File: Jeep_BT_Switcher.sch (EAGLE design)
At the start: 26 parts, among them J1 MF-CON-2.54mm-01x06, J2 MF-CON-2.54mm-01x04, U1 AZ4558C, U2 MAX4544CSA+, U3 MAX4544CSA+

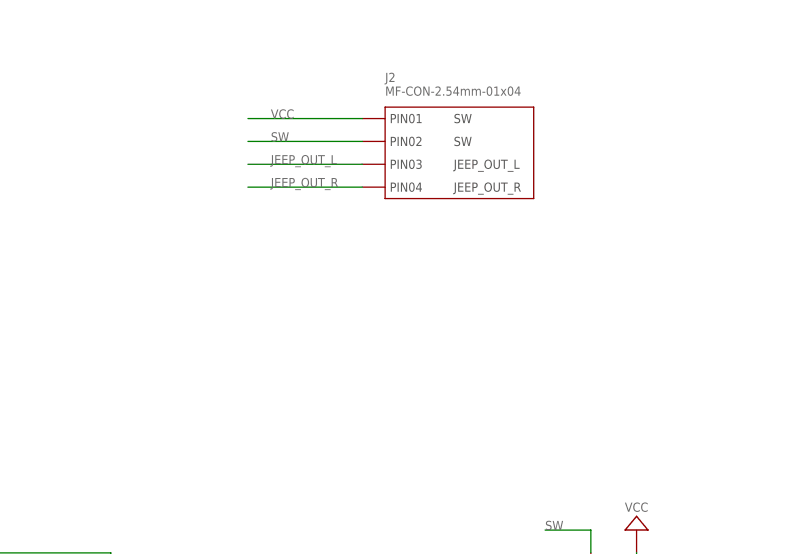
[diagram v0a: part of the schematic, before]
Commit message: Added EXT power connector.
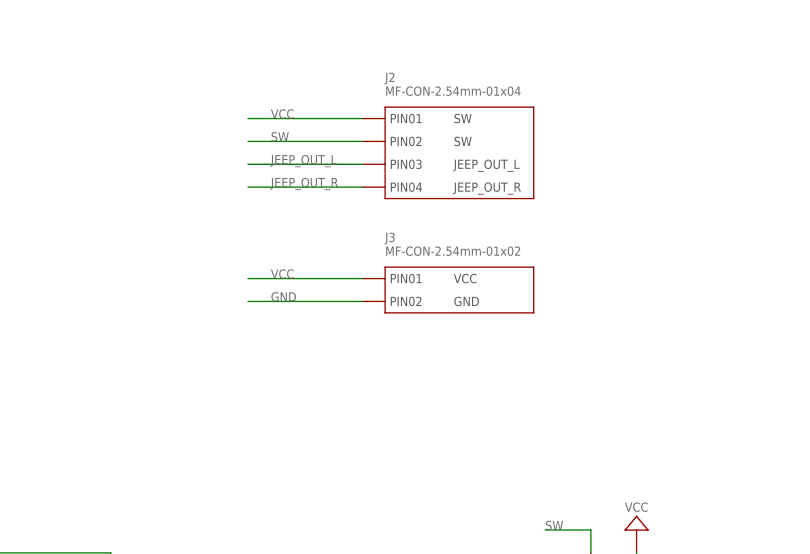
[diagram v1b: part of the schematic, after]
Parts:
- added J3: MF-CON-2.54mm-01x02, MF_Connectors:CON_01X02_PTH_2.54MM
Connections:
- net GND: now also J3.PIN2
- net VCC: now also J3.PIN1
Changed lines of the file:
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@@
 <part name="H4" library="PP_Connectors" deviceset="MOUNT_HOLE" device="150MIL"/>
 <part name="C7" library="MF_Passives" deviceset="CAPACITOR_NP" device="_0805" value="0.1uF"/>
+<part name="J3" library="MF_Connectors" deviceset="CON_01X02" device="_PTH_2.54MM" value="MF-CON-2.54mm-01x02">
+<attribute name="LABEL01" value="VCC"/>
+<attribute name="LABEL02" value="GND"/>
+</part>
 </parts>
 <sheets>
@@
 <instance part="H4" gate="G$1" x="203.2" y="58.42"/>
 <instance part="C7" gate="G$1" x="7.62" y="86.36" rot="MR0"/>
+<instance part="J3" gate="G$1" x="99.06" y="124.46"/>
 </instances>
 <busses>
@@
 <junction x="127" y="35.56"/>
 <label x="129.54" y="35.56" size="1.016" layer="95" font="vector"/>
+</segment>
+<segment>
+<pinref part="J3" gate="G$1" pin="PIN1"/>
+<wire x1="96.52" y1="124.46" x2="83.82" y2="124.46" width="0.1524" layer="91"/>
+<label x="86.36" y="124.46" size="1.016" layer="95" font="vector"/>
 </segment>
 </net>
@@
 <label x="129.54" y="17.78" size="1.016" layer="95" font="vector"/>
 </segment>
+<segment>
+<pinref part="J3" gate="G$1" pin="PIN2"/>
+<wire x1="83.82" y1="121.92" x2="96.52" y2="121.92" width="0.1524" layer="91"/>
+<label x="86.36" y="121.92" size="1.016" layer="95" font="vector"/>
+</segment>
 </net>

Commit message: Added cam files and XYRS
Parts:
- added U$11: LHE_FRAME, PP_Aesthetics:LHE_FRAME
- added U$12: MF_LOGOLOGO_SMALL, PP_Aesthetics:MF_LOGOLOGO_SMALL
- added U$13: LHE_LOGOLHE_LOGO, PP_Aesthetics:LHE_LOGOLHE_LOGO
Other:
- moved on the sheet: C1, C2, C3, C4, C5, C6, C7, H1, H2, H3, H4, J1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

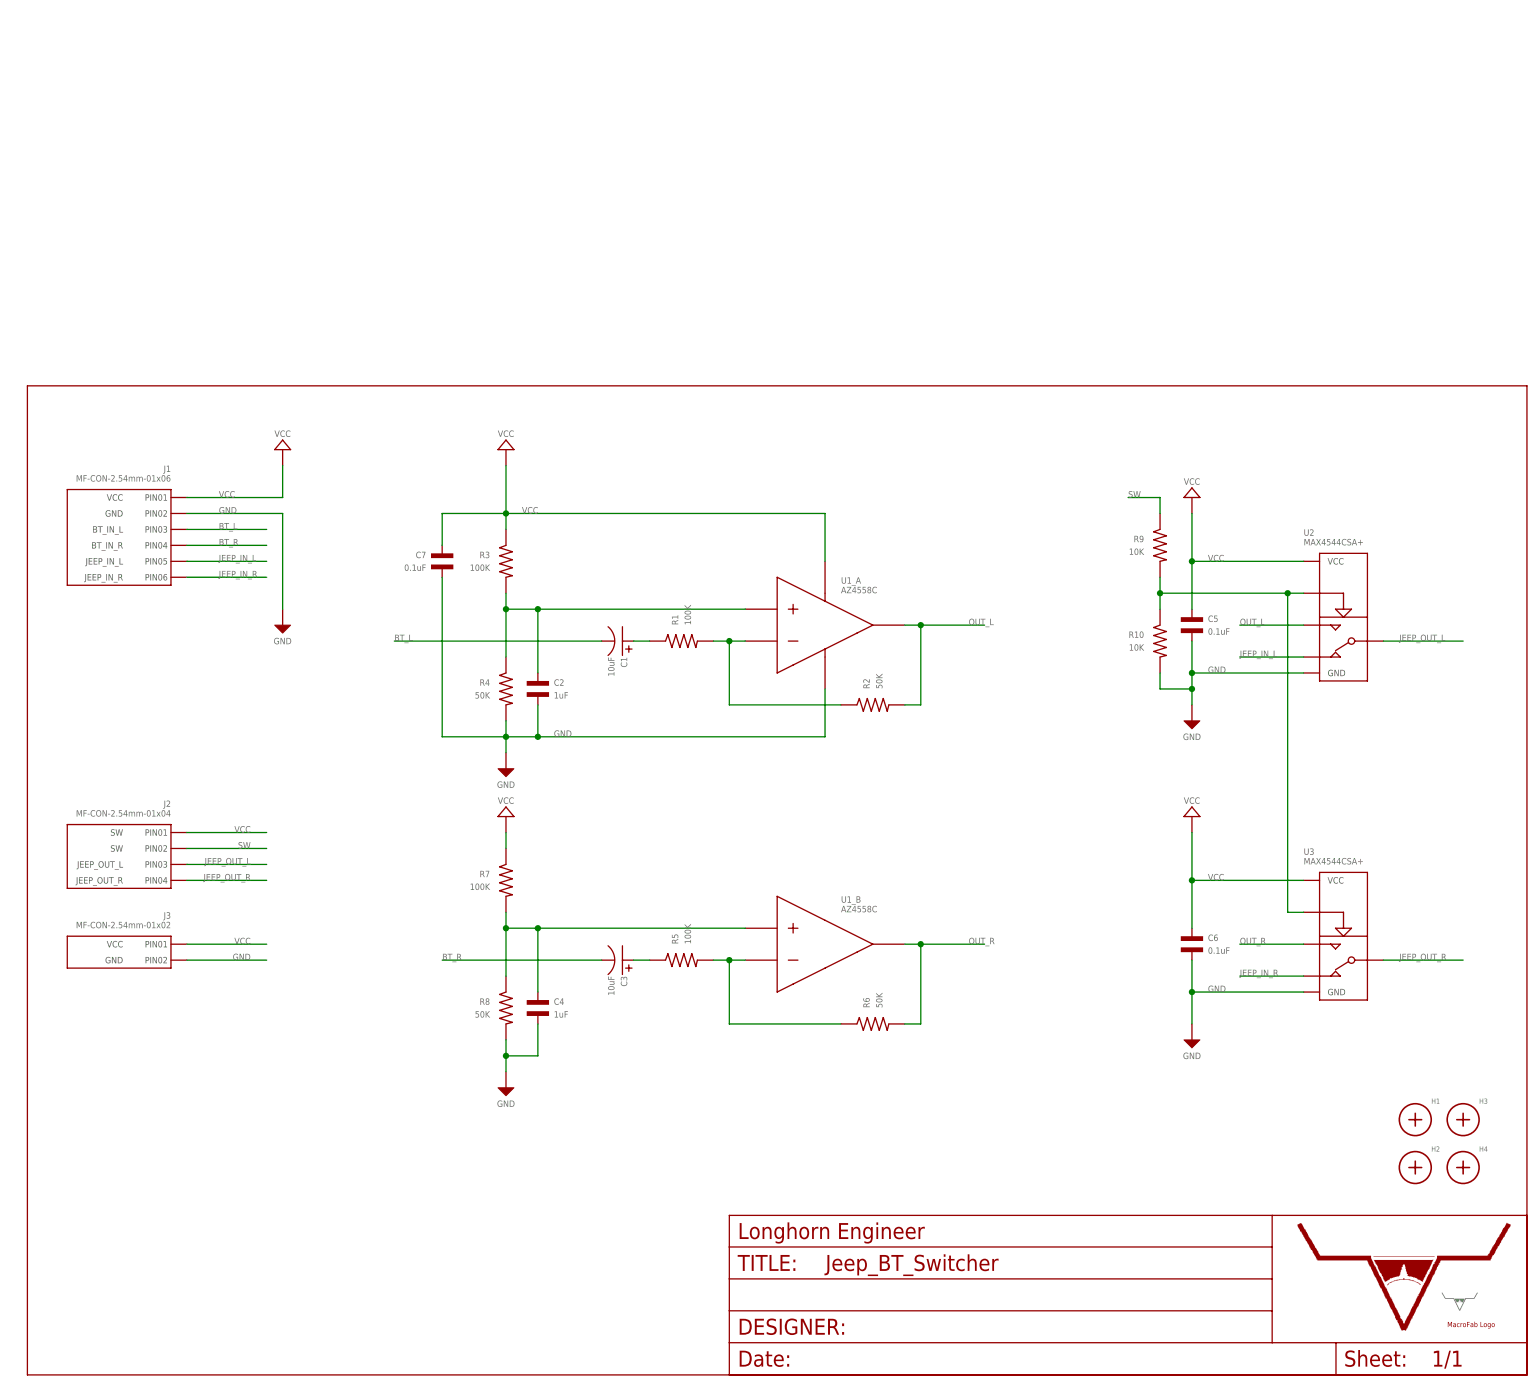
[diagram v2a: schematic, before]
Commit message: Adding built in BT module.
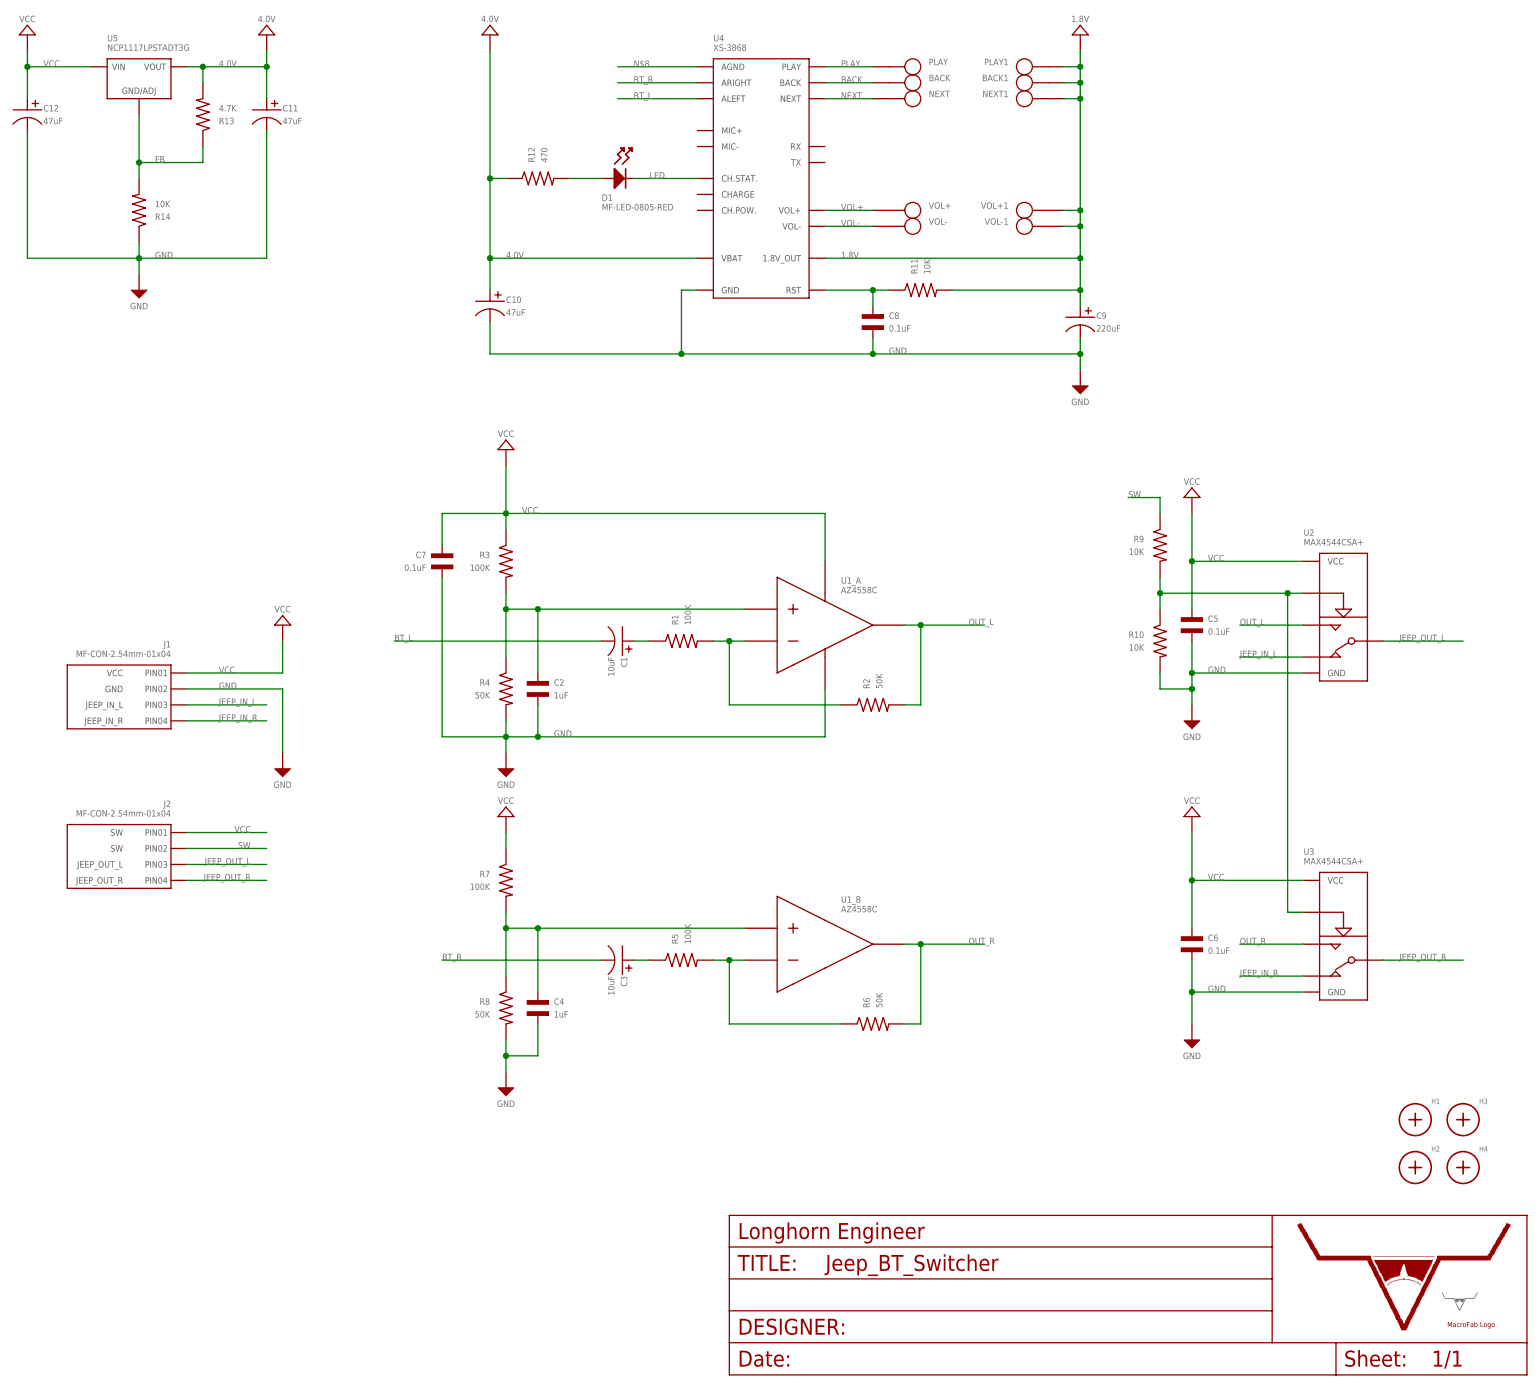
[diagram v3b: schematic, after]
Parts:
- removed J3: MF-CON-2.54mm-01x02, MF_Connectors:CON_01X02_PTH_2.54MM
- added BACK, BACK1, NEXT, NEXT1, PLAY, PLAY1, VOL+, VOL+1, VOL-, VOL-1: (no value), PP_Connectors:TEST_POINT_SINGLE_ROUND_1MM
- added C10, C11, C12: 47uF, MF_Passives:CAPACITOR_P_6.3MM
- added C8: 0.1uF, MF_Passives:CAPACITOR_NP_0805
- added C9: 220uF, MF_Passives:CAPACITOR_P_10MM
- added D1: MF-LED-0805-RED, MF_LEDs:LED_SINGLE-0805-RED
- added R11, R14: 10K, MF_Passives:RESISTOR_0805
- added R12: 470, MF_Passives:RESISTOR_0805
- added R13: 4.7K, MF_Passives:RESISTOR_0805
- added U4: XS-3868, PP_Sensors:XS3868
- added U5: NCP1117LPSTADT3G, MF_IC_Power:NCP1117LPSTADT3G
- J1: value MF-CON-2.54mm-01x06 -> MF-CON-2.54mm-01x04; device MF_Connectors:CON_01X06_PTH_2.54MM -> MF_Connectors:CON_01X04_PTH_2.54MM; LABEL03 BT_IN_L -> JEEP_IN_L; LABEL04 BT_IN_R -> JEEP_IN_R; LABEL05 JEEP_IN_L -> (none); LABEL06 JEEP_IN_R -> (none)
- U$11: REVNUM REV: 2 -> REV: 3
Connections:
- new net 1.8V: BACK1.P$1, C9.P$1, NEXT1.P$1, PLAY1.P$1, R11.P$2, U4.1.8V_OUT, VOL+1.P$1, VOL-1.P$1
- new net 4.0V: C10.P$1, C11.P$1, R12.P$1, R13.P$2, U4.VBAT, U5.VOUT
- new net BACK: BACK.P$1, U4.BACK
- new net FB: R13.P$1, R14.P$2, U5.GND/ADJ
- new net LED: D1.CATHODE, U4.CH.STAT.
- new net N$10: D1.ANODE, R12.P$2
- new net N$8: U4.AGND
- new net NEXT: NEXT.P$1, U4.NEXT
- new net PLAY: PLAY.P$1, U4.PLAY
- new net RST: C8.P$1, R11.P$1, U4.RST
- new net VOL+: U4.VOL+, VOL+.P$1
- new net VOL-: U4.VOL-, VOL-.P$1
- net BT_L: now also U4.ALEFT; no longer J1.PIN3
- net BT_R: now also U4.ARIGHT; no longer J1.PIN4
- net GND: now also C10.P$2, C11.P$2, C12.P$2, C8.P$2, C9.P$2, R14.P$1, U4.GND; no longer J3.PIN2
- net JEEP_IN_L: now also J1.PIN3; no longer J1.PIN5
- net JEEP_IN_R: now also J1.PIN4; no longer J1.PIN6
- net VCC: now also C12.P$1, U5.VIN; no longer J3.PIN1
